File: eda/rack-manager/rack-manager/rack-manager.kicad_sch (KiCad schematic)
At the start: 96 parts, among them J1 Screw_Terminal_01x02, J10 Screw_Terminal_01x02, J11 Conn_02x03_Odd_Even, J12 Conn_01x02_Pin, J13 Conn_01x04_Socket, J16 Conn_01x04_Socket, J17 Conn_01x04_Socket, J18 Conn_01x04_Socket, J19 Conn_01x04_Socket, J2 Screw_Terminal_01x02, J20 Conn_01x04_Socket, J21 Conn_01x04_Socket, J22 Conn_01x04_Socket, J23 Conn_01x04_Socket, J24 Conn_02x06_Odd_Even, J25 Conn_02x06_Odd_Even, J3 Screw_Terminal_01x02, J4 Screw_Terminal_01x02, J5 Screw_Terminal_01x02, J6 Screw_Terminal_01x02, J7 Screw_Terminal_01x02, J8 Screw_Terminal_01x02, J9 Screw_Terminal_01x02, SW1 SW_Push, U1 ADS131M02IRUKR, U2 ADS131M02IRUKR, U3 ADS131M02IRUKR, U5 TCA9548AMRGER, U6 PCA9555PW

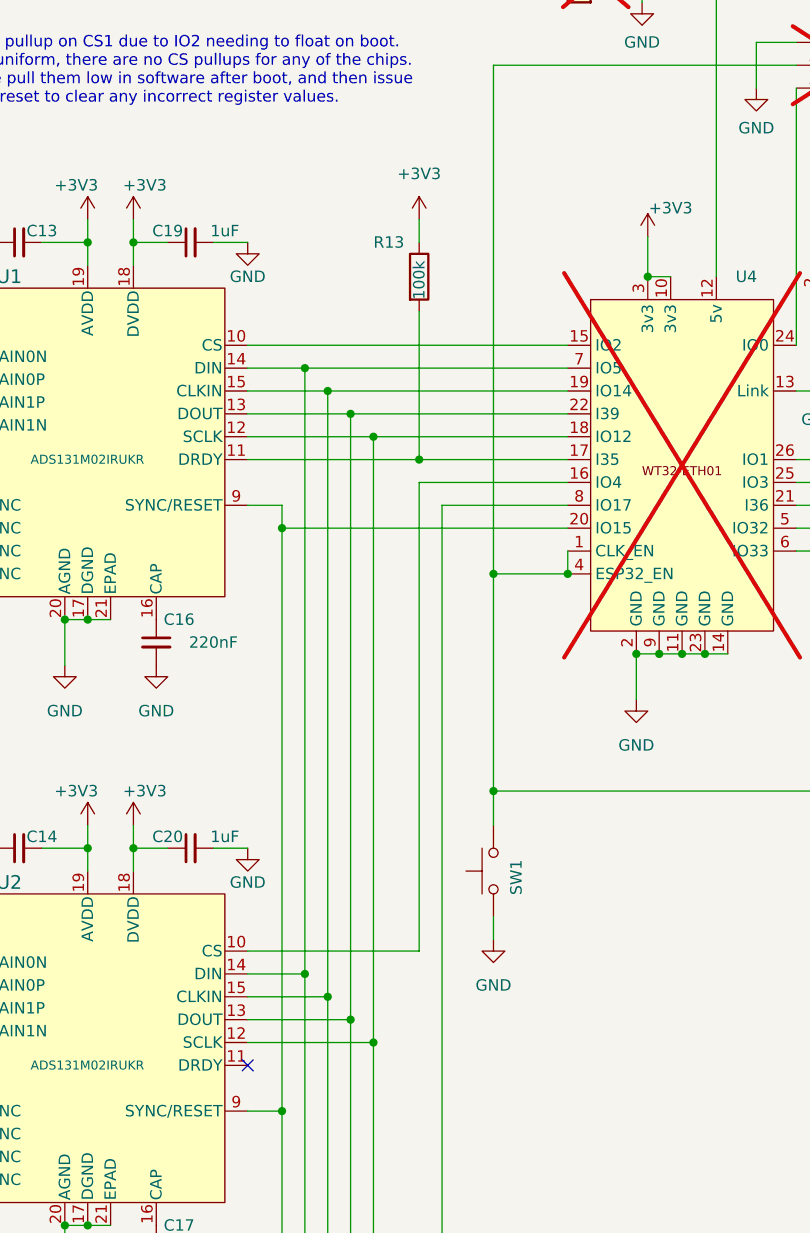
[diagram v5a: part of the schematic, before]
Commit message: Rack manager board routing
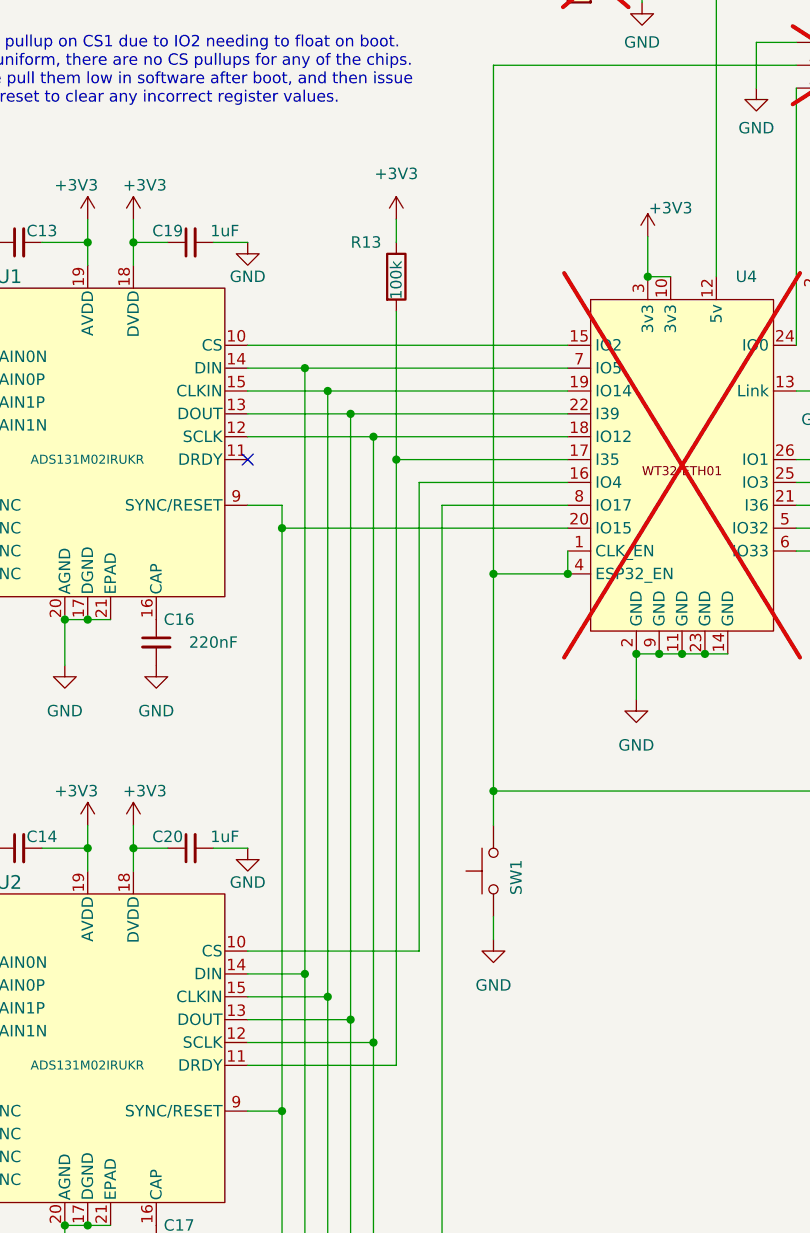
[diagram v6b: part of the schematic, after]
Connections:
- net at R13.2, U4.17 (I35): now also U2.11 (DRDY); no longer U1.11 (DRDY)
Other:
- moved on the sheet: R13
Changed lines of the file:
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@@
 	)
 	(junction
-		(at 147.32 84.455)
-		(diameter 0)
-		(color 0 0 0 0)
-	)
-	(junction
 		(at 319.79 96.52)
 		(diameter 0)
@@
 	)
 	(junction
+		(at 144.78 84.455)
+		(diameter 0)
+		(color 0 0 0 0)
+	)
+	(junction
 		(at 171.45 106.045)
 		(diameter 0)
@@
 	)
 	(no_connect
-		(at 128.27 219.075)
+		(at 128.27 84.455)
 	)
 	(no_connect
-		(at 128.27 151.765)
+		(at 128.27 219.075)
 	)
 	(bus_entry
@@
 	(wire
 		(pts
+			(xy 144.78 151.765) (xy 144.78 84.455)
+		)
+		(stroke
+			(width 0)
+			(type default)
+		)
+	)
+	(wire
+		(pts
 			(xy 128.27 211.455) (xy 137.16 211.455)
 		)
@@
 	(wire
 		(pts
+			(xy 128.27 151.765) (xy 144.78 151.765)
+		)
+		(stroke
+			(width 0)
+			(type default)
+		)
+	)
+	(wire
+		(pts
 			(xy 110.49 60.325) (xy 110.49 57.785)
 		)
@@
 	(wire
 		(pts
-			(xy 147.32 57.785) (xy 147.32 60.325)
+			(xy 144.78 57.785) (xy 144.78 60.325)
 		)
 		(stroke
@@
 	(wire
 		(pts
-			(xy 147.32 67.945) (xy 147.32 84.455)
+			(xy 144.78 67.945) (xy 144.78 84.455)
 		)
 		(stroke
@@
 	(wire
 		(pts
-			(xy 147.32 84.455) (xy 163.83 84.455)
+			(xy 144.78 84.455) (xy 163.83 84.455)
 		)
 		(stroke
@@
 	(wire
 		(pts
-			(xy 128.27 84.455) (xy 147.32 84.455)
-		)
-		(stroke
-			(width 0)
-			(type default)
-		)
-	)
-	(wire
-		(pts
 			(xy 286.9907 124.46) (xy 286.9907 134.62)
 		)
@@
 	(symbol
 		(lib_id "Device:R")
-		(at 147.32 64.135 0)
+		(at 144.78 64.135 0)
 		(unit 1)
 		(body_style 1)
@@
 		(dnp no)
 		(property "Reference" "R13"
-			(at 142.24 60.325 0)
+			(at 139.7 60.325 0)
 			(show_name no)
 			(do_not_autoplace no)
@@
 		)
 		(property "Value" "100k"
-			(at 147.32 66.675 90)
+			(at 144.78 66.675 90)
 			(show_name no)
 			(do_not_autoplace no)
@@
 		)
 		(property "Footprint" "Resistor_SMD:R_0603_1608Metric"
-			(at 145.542 64.135 90)
+			(at 143.002 64.135 90)
 			(hide yes)
 			(show_name no)
@@
 		)
 		(property "Datasheet" "0603WAF1003T5E"
-			(at 147.32 64.135 0)
+			(at 144.78 64.135 0)
 			(hide yes)
 			(show_name no)
@@
 		)
 		(property "Description" "Resistor"
-			(at 147.32 64.135 0)
+			(at 144.78 64.135 0)
 			(hide yes)
 			(show_name no)
@@
 		)
 		(property "LCSC" "C25803"
-			(at 147.32 66.675 90)
+			(at 144.78 66.675 90)
 			(hide yes)
 			(show_name no)
@@
 	(symbol
 		(lib_id "power:+3V3")
-		(at 147.32 57.785 0)
+		(at 144.78 57.785 0)
 		(unit 1)
 		(body_style 1)
@@
 		(fields_autoplaced yes)
 		(property "Reference" "#PWR025"
-			(at 147.32 61.595 0)
+			(at 144.78 61.595 0)
 			(hide yes)
 			(show_name no)
@@
 		)
 		(property "Value" "+3V3"
-			(at 147.32 52.705 0)
+			(at 144.78 52.705 0)
 			(show_name no)
 			(do_not_autoplace no)
@@
 		)
 		(property "Footprint" ""
-			(at 147.32 57.785 0)
+			(at 144.78 57.785 0)
 			(hide yes)
 			(show_name no)
@@
 		)
 		(property "Datasheet" ""
-			(at 147.32 57.785 0)
+			(at 144.78 57.785 0)
 			(hide yes)
 			(show_name no)
@@
 		)
 		(property "Description" "Power symbol creates a global label with name \"+3V3\""
-			(at 147.32 57.785 0)
+			(at 144.78 57.785 0)
 			(hide yes)
 			(show_name no)

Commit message: More routing
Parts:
- J12: footprint Connector_PinHeader_1.00mm:PinHeader_1x02_P1.00mm_Vertical -> Connector_PinHeader_2.54mm:PinHeader_1x02_P2.54mm_Vertical
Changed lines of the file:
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@@
 			)
 		)
-		(property "Footprint" "Connector_PinHeader_1.00mm:PinHeader_1x02_P1.00mm_Vertical"
+		(property "Footprint" "Connector_PinHeader_2.54mm:PinHeader_1x02_P2.54mm_Vertical"
 			(at 194.31 61.595 0)
 			(hide yes)

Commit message: Silkscreen
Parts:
- SW1: value SW_Push -> C720477
- renumbered U2 to ADC1, U3 to ADC2, U1 to ADC3
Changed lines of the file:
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@@
 		(in_pos_files yes)
 		(dnp no)
-		(property "Reference" "U3"
+		(property "Reference" "ADC2"
 			(at 100.33 198.755 0)
 			(show_name no)
@@
 			(project "rack-manager"
 				(path "/b46e9a14-8827-41a7-9091-cc2dee17597f"
-					(reference "U3")
+					(reference "ADC2")
 					(unit 1)
 				)
@@
 			)
 		)
-		(property "Value" "SW_Push"
+		(property "Value" "C720477"
 			(at 153.035 131.445 0)
 			(hide yes)
@@
 		(in_pos_files yes)
 		(dnp no)
-		(property "Reference" "U2"
+		(property "Reference" "ADC1"
 			(at 100.33 131.445 0)
 			(show_name no)
@@
 			(project "rack-manager"
 				(path "/b46e9a14-8827-41a7-9091-cc2dee17597f"
-					(reference "U2")
+					(reference "ADC1")
 					(unit 1)
 				)
@@
 		(in_pos_files yes)
 		(dnp no)
-		(property "Reference" "U1"
+		(property "Reference" "ADC3"
 			(at 100.33 64.135 0)
 			(show_name no)
@@
 			(project "rack-manager"
 				(path "/b46e9a14-8827-41a7-9091-cc2dee17597f"
-					(reference "U1")
+					(reference "ADC3")
 					(unit 1)
 				)
